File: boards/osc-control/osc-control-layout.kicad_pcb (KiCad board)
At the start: 4 copper layers, 316 x 116 mm, 454 parts, among them J900052 BM03B-GHS-TBT(LF)(SN), J900054 BM03B-GHS-TBT(LF)(SN), J900056 BM03B-GHS-TBT(LF)(SN), J900058 BM03B-GHS-TBT(LF)(SN), J900134 BM03B-GHS-TBT(LF)(SN), J900136 BM03B-GHS-TBT(LF)(SN), J900138 BM03B-GHS-TBT(LF)(SN), J900140 BM03B-GHS-TBT(LF)(SN), J900142 BM03B-GHS-TBT(LF)(SN), J900144 BM03B-GHS-TBT(LF)(SN), J900146 BM03B-GHS-TBT(LF)(SN), J900148 BM03B-GHS-TBT(LF)(SN), J900150 BM03B-GHS-TBT(LF)(SN), J900152 BM03B-GHS-TBT(LF)(SN), J900154 BM03B-GHS-TBT(LF)(SN), J900156 BM03B-GHS-TBT(LF)(SN), J900158 BM03B-GHS-TBT(LF)(SN), J900160 BM03B-GHS-TBT(LF)(SN), J900162 BM03B-GHS-TBT(LF)(SN), J900164 BM03B-GHS-TBT(LF)(SN), J900166 BM03B-GHS-TBT(LF)(SN), J900168 BM03B-GHS-TBT(LF)(SN), J900170 BM03B-GHS-TBT(LF)(SN), J900172 BM03B-GHS-TBT(LF)(SN), J900174 BM03B-GHS-TBT(LF)(SN), J900176 BM03B-GHS-TBT(LF)(SN), J900178 BM03B-GHS-TBT(LF)(SN), J900180 BM03B-GHS-TBT(LF)(SN), J900182 BM03B-GHS-TBT(LF)(SN), J900184 BM03B-GHS-TBT(LF)(SN), J900186 BM03B-GHS-TBT(LF)(SN), J900188 BM03B-GHS-TBT(LF)(SN), J900190 BM03B-GHS-TBT(LF)(SN), J900192 BM03B-GHS-TBT(LF)(SN), J900194 BM03B-GHS-TBT(LF)(SN), J900196 BM03B-GHS-TBT(LF)(SN), J900198 BM03B-GHS-TBT(LF)(SN), J900200 BM03B-GHS-TBT(LF)(SN), J900202 BM03B-GHS-TBT(LF)(SN), J900204 BM03B-GHS-TBT(LF)(SN), J900206 BM03B-GHS-TBT(LF)(SN), J900208 BM03B-GHS-TBT(LF)(SN), J900210 BM03B-GHS-TBT(LF)(SN), J900212 BM03B-GHS-TBT(LF)(SN), J900214 BM03B-GHS-TBT(LF)(SN), J900216 BM03B-GHS-TBT(LF)(SN), J900218 BM03B-GHS-TBT(LF)(SN), J900220 BM03B-GHS-TBT(LF)(SN), J900222 BM03B-GHS-TBT(LF)(SN), J900224 BM03B-GHS-TBT(LF)(SN), J900226 BM03B-GHS-TBT(LF)(SN), J900228 BM03B-GHS-TBT(LF)(SN), J900230 BM03B-GHS-TBT(LF)(SN), J900232 BM03B-GHS-TBT(LF)(SN), J900234 BM03B-GHS-TBT(LF)(SN), J900236 BM03B-GHS-TBT(LF)(SN), J900238 BM03B-GHS-TBT(LF)(SN), J900240 BM03B-GHS-TBT(LF)(SN), J900242 BM03B-GHS-TBT(LF)(SN), J900244 BM03B-GHS-TBT(LF)(SN), J900246 BM03B-GHS-TBT(LF)(SN), J900248 BM03B-GHS-TBT(LF)(SN), J900250 BM03B-GHS-TBT(LF)(SN), J900252 BM03B-GHS-TBT(LF)(SN), J900254 BM03B-GHS-TBT(LF)(SN), J900256 BM03B-GHS-TBT(LF)(SN), J900258 BM03B-GHS-TBT(LF)(SN), J900260 BM03B-GHS-TBT(LF)(SN), J900262 BM03B-GHS-TBT(LF)(SN), J900264 BM03B-GHS-TBT(LF)(SN), J900266 BM03B-GHS-TBT(LF)(SN), J900268 BM03B-GHS-TBT(LF)(SN), J900270 BM03B-GHS-TBT(LF)(SN), J900272 BM03B-GHS-TBT(LF)(SN), J900274 BM03B-GHS-TBT(LF)(SN), J900276 BM03B-GHS-TBT(LF)(SN), J900278 BM03B-GHS-TBT(LF)(SN), J900280 BM03B-GHS-TBT(LF)(SN), J900282 BM03B-GHS-TBT(LF)(SN), J900284 BM03B-GHS-TBT(LF)(SN)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

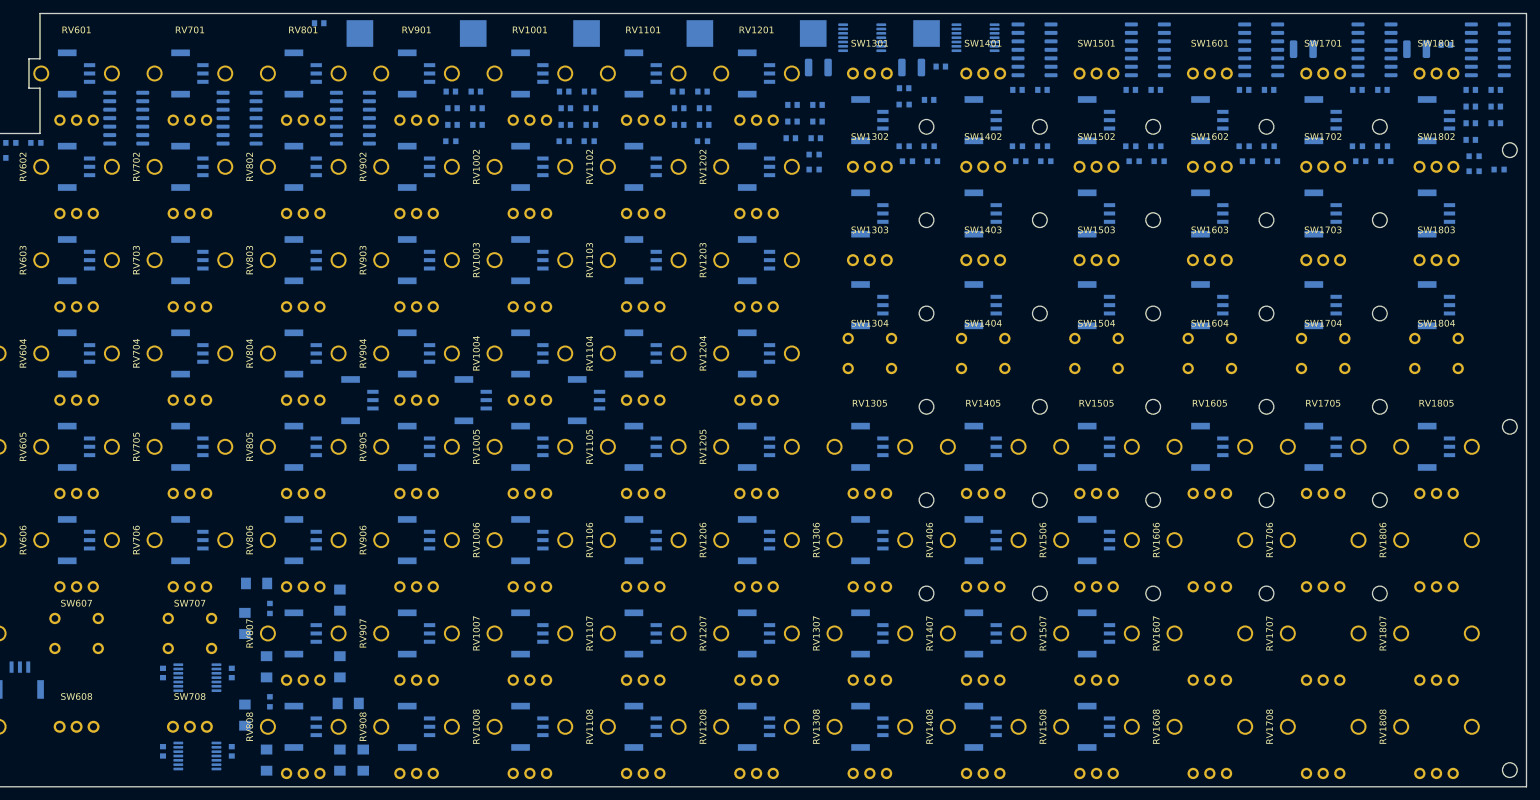
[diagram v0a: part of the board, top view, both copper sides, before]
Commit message: Keep control-board bypass groups local and connect their supply loops
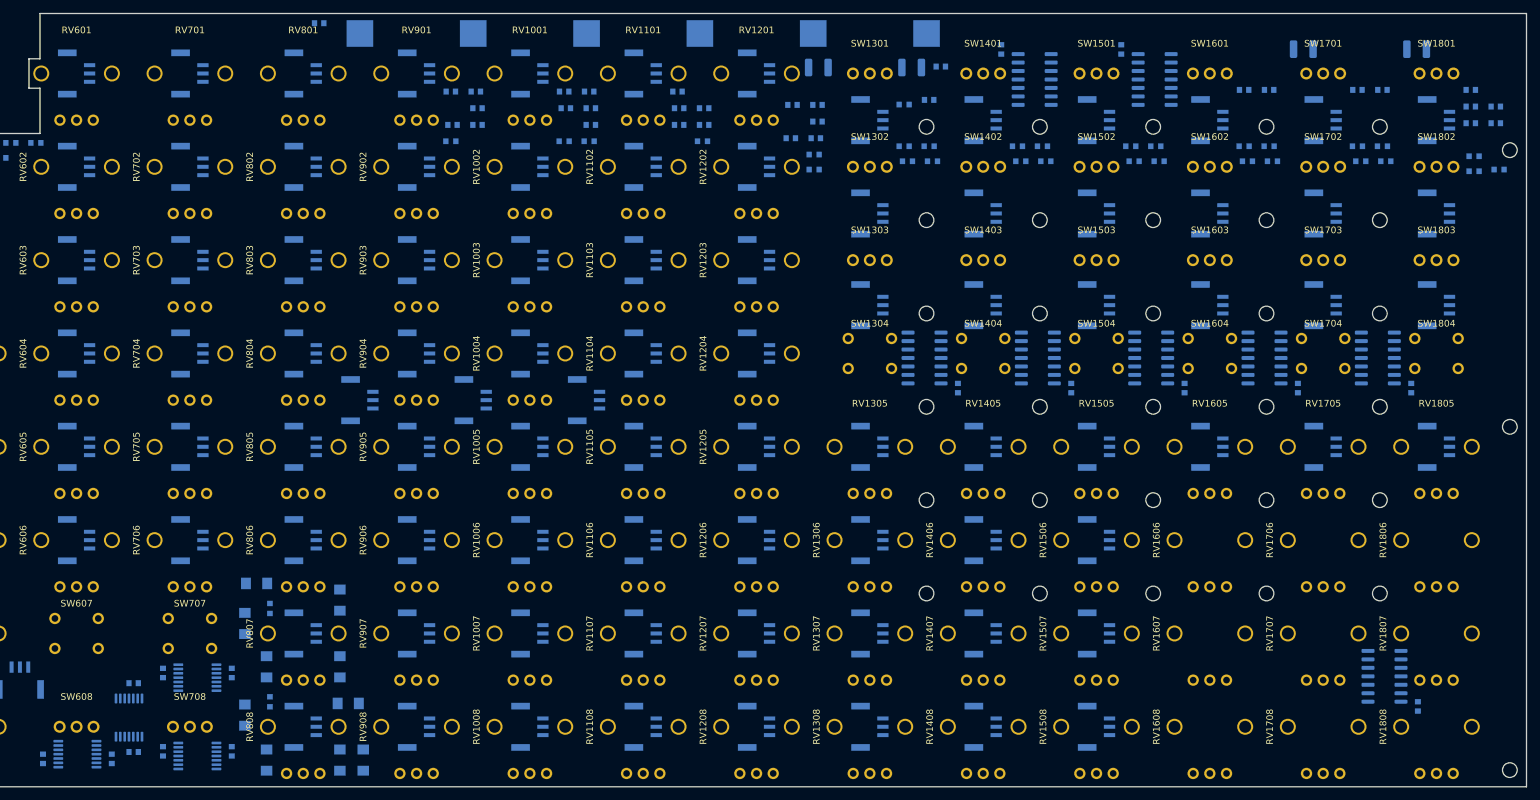
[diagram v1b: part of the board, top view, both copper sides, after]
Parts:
- moved U4411 191.2 mm to (394.7, 277.7), turned to 0 degrees
- moved C3406 179.6 mm to (208.1, 336.8), turned to 0 degrees
- moved C3306 177.3 mm to (194.5, 337.8), turned to -90 degrees
- moved C3407 177.3 mm to (208.1, 326.5), turned to 0 degrees
- moved U4611 175.9 mm to (395.7, 325.4), turned to 0 degrees
- moved C3307 171.9 mm to (204.8, 337.8), turned to -90 degrees
- moved U3403 162.9 mm to (207.4, 331.6), turned to 90 degrees
- moved U3303 159.4 mm to (199.6, 337.1), turned to 0 degrees
- moved U4511 137.4 mm to (361.2, 235.9)
- moved C4356 133.6 mm to (382.7, 282.2), turned to -90 degrees
- moved C4456 101.1 mm to (399.7, 282.2), turned to -90 degrees
- moved C130 89.5 mm to (331.7, 282.2), turned to -90 degrees
- moved C4656 85.3 mm to (400.7, 329.9), turned to -90 degrees
- moved C4256 84.9 mm to (365.7, 282.2), turned to -90 degrees
- moved C4556 84.1 mm to (356.2, 231.4), turned to 90 degrees
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
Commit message: Reassign paired control connectors and rebuild the routing seed
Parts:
- moved J900204 243.0 mm to (388.4, 242.0)
- moved J900200 240.6 mm to (354.4, 256.0)
- moved J900206 238.0 mm to (405.4, 291.0)
- moved J900202 226.4 mm to (354.4, 242.0)
- moved J900316 225.0 mm to (133.4, 291.0)
- moved J900184 223.8 mm to (405.4, 242.0)
- moved J900208 223.8 mm to (405.4, 256.0)
- moved J900178 221.1 mm to (354.4, 269.8)
- moved J900176 221.1 mm to (337.4, 269.8)
- moved J900314 218.0 mm to (133.4, 256.0)
- moved J900362 204.5 mm to (184.4, 256.0)
- moved J900350 192.8 mm to (184.4, 333.0)
- moved J900312 189.1 mm to (133.4, 305.0)
- moved J900358 188.2 mm to (184.4, 277.0)
- moved J900360 187.0 mm to (184.4, 268.5)
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
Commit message: Localize envelope debounce networks and continue control routing
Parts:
- moved R4623 295.9 mm to (388.0, 329.5), turned to 90 degrees
- moved R4628 293.1 mm to (404.5, 321.0), turned to 90 degrees
- moved R4627 292.6 mm to (392.0, 315.5), turned to -90 degrees
- moved R4423 287.1 mm to (391.5, 287.5), turned to 90 degrees
- moved R4629 286.4 mm to (401.5, 320.5)
- moved R4630 281.4 mm to (407.0, 329.5), turned to -90 degrees
- moved R4631 275.3 mm to (404.0, 331.0)
- moved R4424 268.6 mm to (386.5, 282.0)
- moved R4425 264.5 mm to (386.5, 279.5), turned to 0 degrees
- moved R4426 259.0 mm to (395.5, 266.5), turned to -90 degrees
- moved R4427 252.4 mm to (392.5, 267.5)
- moved R4428 251.5 mm to (403.5, 280.5)
- moved R4429 247.4 mm to (403.5, 277.5), turned to 90 degrees
- moved R4122 227.8 mm to (353.0, 227.5)
- moved R4430 226.4 mm to (397.0, 263.5), turned to 0 degrees
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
